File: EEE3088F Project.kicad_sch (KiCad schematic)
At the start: 2 parts, among them J1 Conn_02x16_Odd_Even, J2 Battery IN JST

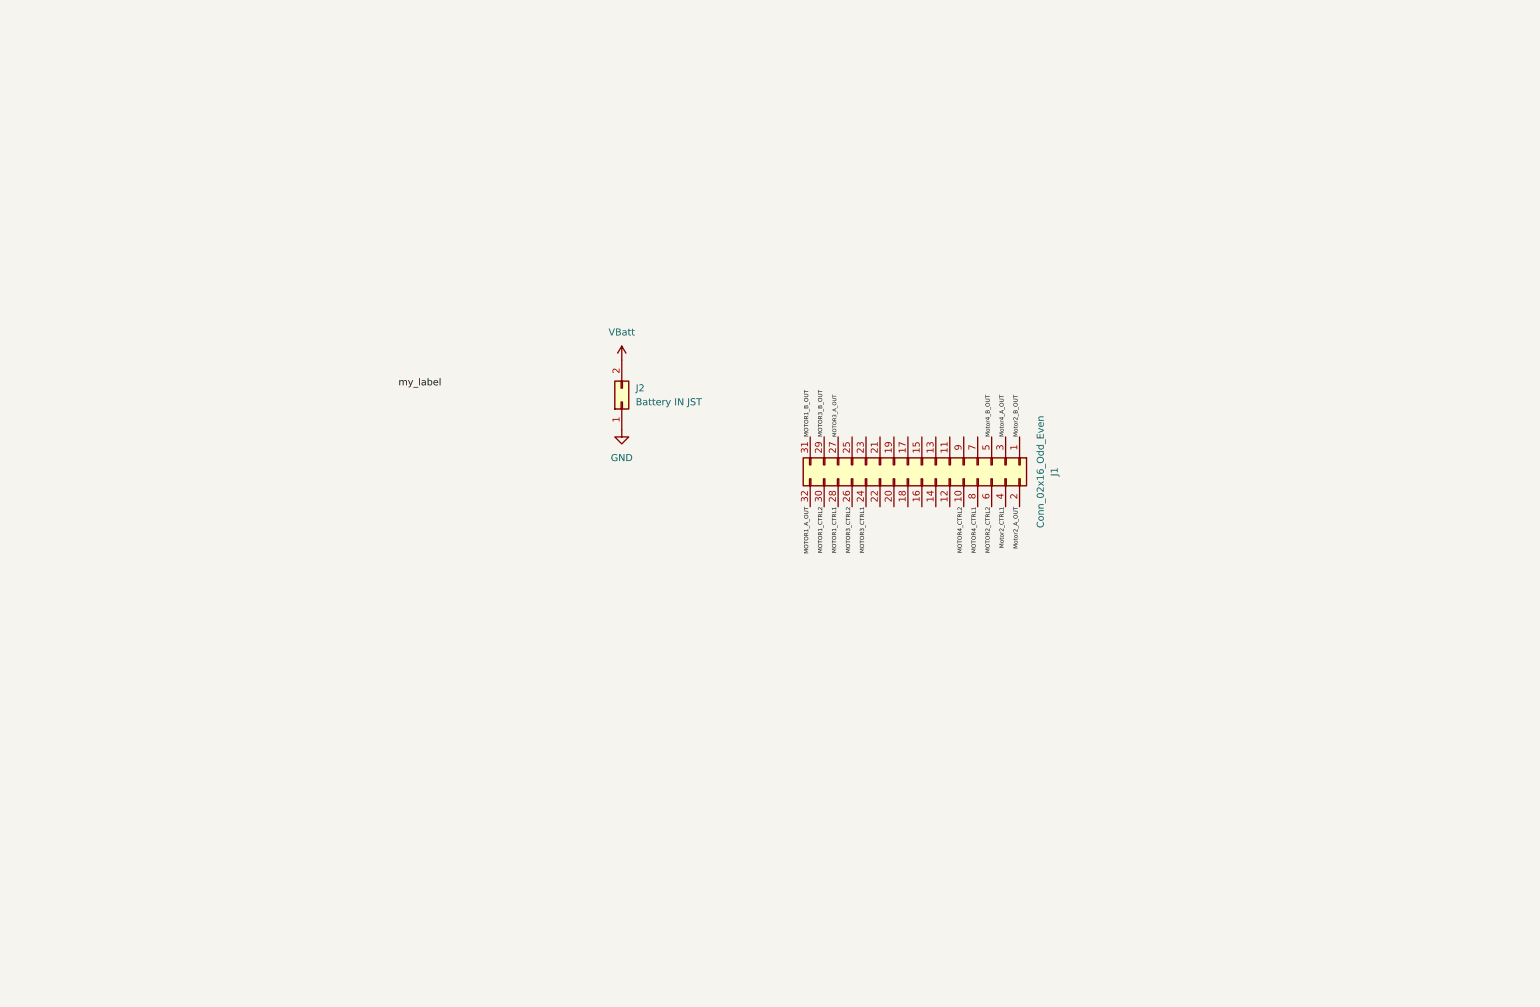
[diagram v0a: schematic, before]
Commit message: added battery charging subsection (no footprints yet)
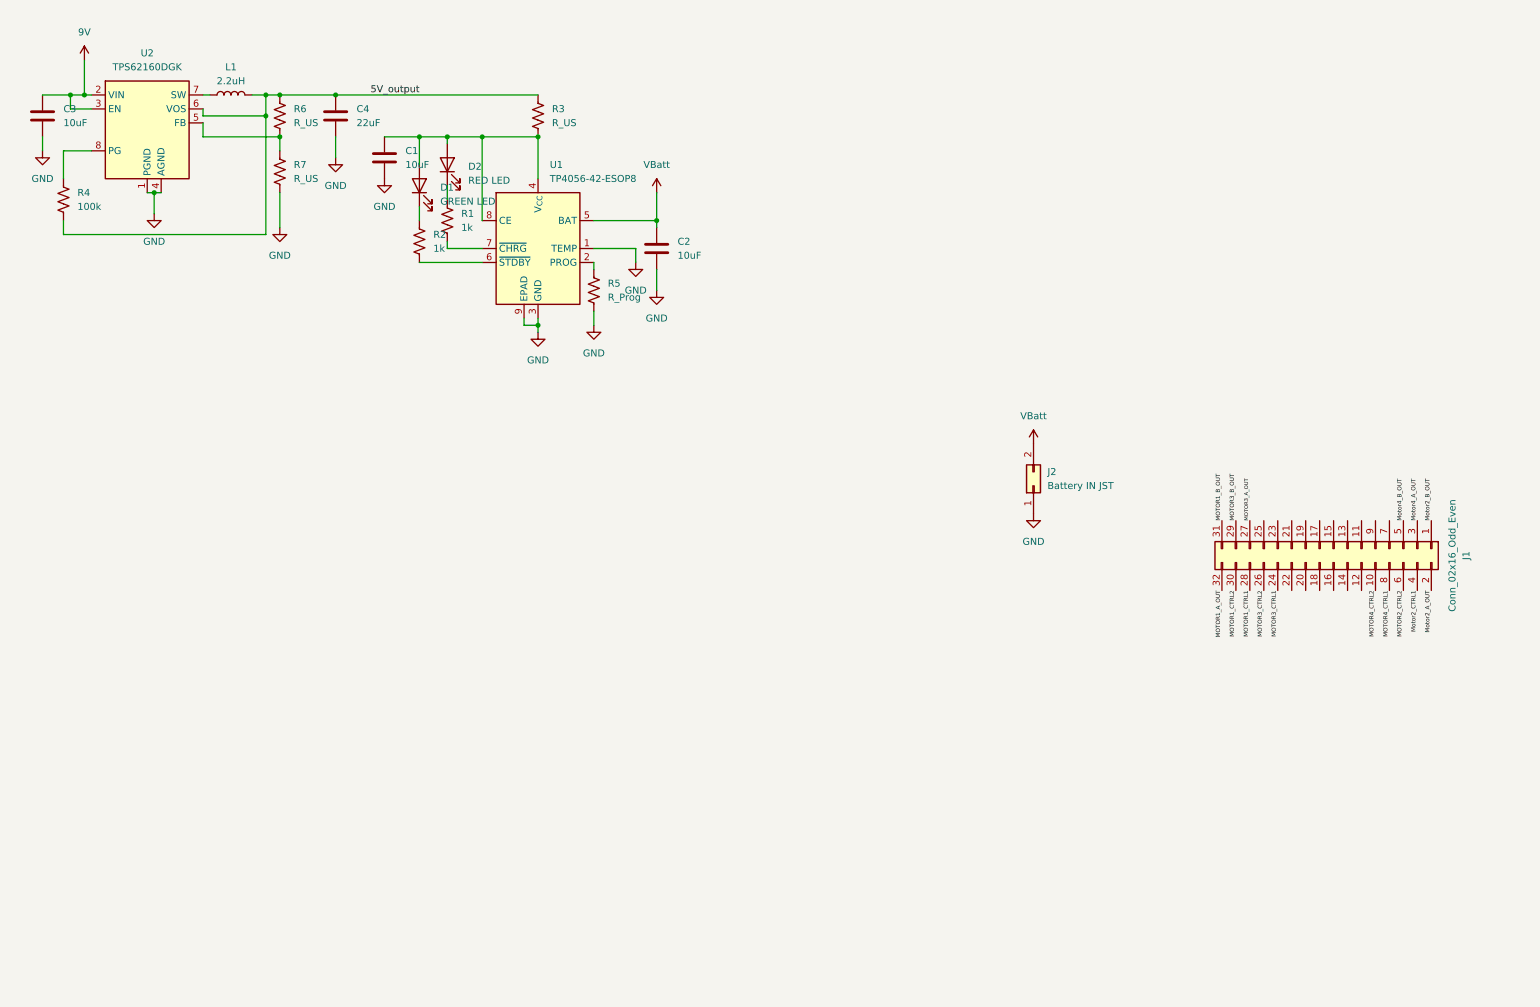
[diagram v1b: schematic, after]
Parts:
- added C1, C2, C3: 10uF, symbol Device:C
- added C4: 22uF, symbol Device:C
- added D1: GREEN LED, symbol Device:LED
- added D2: RED LED, symbol Device:LED
- added L1: 2.2uH, symbol Device:L
- added R1, R2: 1k, symbol Device:R_US
- added R3, R6, R7: R_US, symbol Device:R_US
- added R4: 100k, symbol Device:R_US
- added R5: R_Prog, symbol Device:R_US
- added U1: TP4056-42-ESOP8, Package_SO:SOIC-8-1EP_3.9x4.9mm_P1.27mm_EP2.41x3.3mm_ThermalVias, symbol Battery_Management:TP4056-42-ESOP8
- added U2: TPS62160DGK, Package_SO:MSOP-8_3x3mm_P0.65mm, symbol Regulator_Switching:TPS62160DGK
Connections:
- net GND: now also C1.1, C2.2, C3.2, C4.2, R5.2, R7.2, U1.1 (TEMP), U1.3 (GND), U1.9 (EPAD), U2.1 (PGND), U2.4 (AGND)
- net VBatt: now also C2.1, U1.5 (BAT)
- new net: D2.1 (K), R1.1
- new net: C1.2, D1.2 (A), D2.2 (A), R3.2, U1.4 (V_{CC}), U1.8 (CE)
- new net: R6.2, R7.1, U2.5 (FB)
- new net: R5.1, U1.2 (PROG)
- new net: D1.1 (K), R2.1
- new net: R2.2, U1.6 (~{STDBY})
- new net: L1.1, U2.7 (SW)
- new net: R4.1, U2.8 (PG)
- new net: R1.2, U1.7 (~{CHRG})
- new net 5V_output: C4.1, L1.2, R3.1, R4.2, R6.1, U2.6 (VOS)
- new net 9V: C3.1, U2.2 (VIN), U2.3 (EN)
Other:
- moved on the sheet: J1, J2

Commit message: Added motor driver circuits and footprints
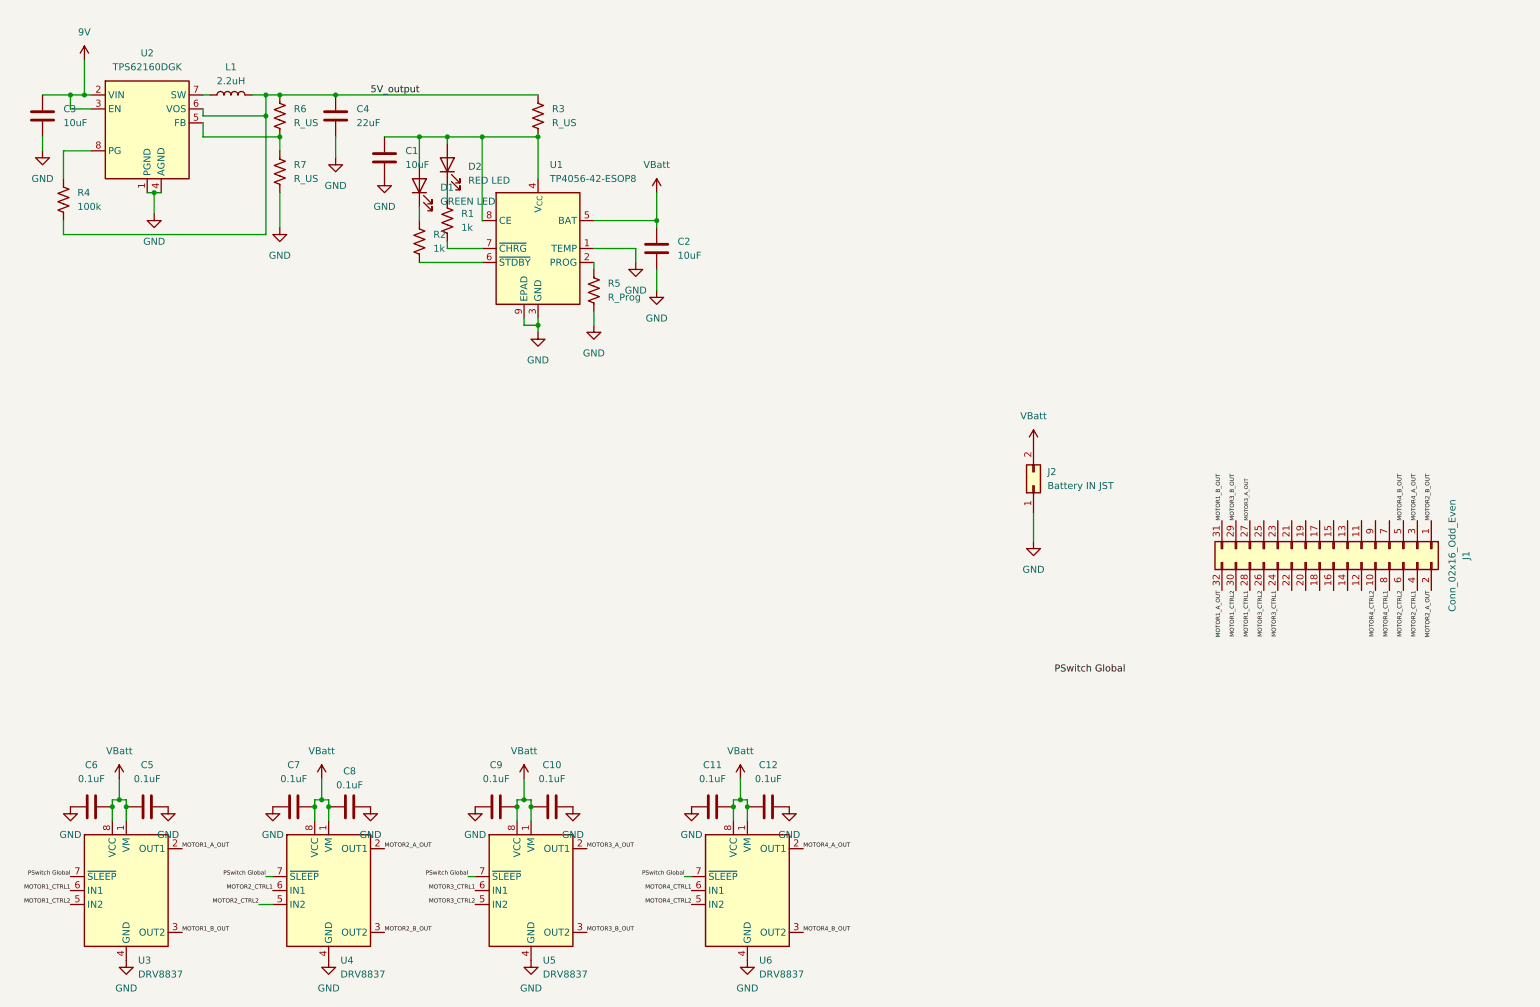
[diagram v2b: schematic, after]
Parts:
- added C10, C11, C12, C5, C6, C7, C8, C9: 0.1uF, Capacitor_SMD:C_0402_1005Metric_Pad0.74x0.62mm_HandSolder, symbol Device:C
- added U3, U4, U5, U6: DRV8837, Package_SON:WSON-8-1EP_2x2mm_P0.5mm_EP0.9x1.6mm, symbol Driver_Motor:DRV8837
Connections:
- net GND: now also C10.2, C11.1, C12.2, C5.2, C6.1, C7.1, C8.2, C9.1, U3.4 (GND), U3.9 (GND), U4.4 (GND), U4.9 (GND), U5.4 (GND), U5.9 (GND), U6.4 (GND), U6.9 (GND)
- net MOTOR1_A_OUT: now also U3.2 (OUT1)
- net MOTOR1_B_OUT : now also U3.3 (OUT2)
- net MOTOR1_CTRL1: now also U3.6 (IN1)
- net MOTOR1_CTRL2: now also U3.5 (IN2)
- net MOTOR3_A_OUT: now also U5.2 (OUT1)
- net MOTOR3_B_OUT : now also U5.3 (OUT2)
- net MOTOR3_CTRL1: now also U5.6 (IN1)
- net MOTOR3_CTRL2: now also U5.5 (IN2)
- net MOTOR4_CTRL2: now also U6.5 (IN2)
- net VBatt: now also C10.1, C11.2, C12.1, C5.1, C6.2, C7.2, C8.1, C9.2, U3.1 (VM), U3.8 (VCC), U4.1 (VM), U4.8 (VCC), U5.1 (VM), U5.8 (VCC), U6.1 (VM), U6.8 (VCC)
- net Motor2_A_OUT renamed MOTOR2_A_OUT
- net MOTOR2_A_OUT: now also U4.2 (OUT1)
- net Motor2_B_OUT renamed MOTOR2_B_OUT
- net Motor2_CTRL1 renamed MOTOR2_CTRL1
- net MOTOR2_CTRL1: now also U4.6 (IN1)
- net Motor4_A_OUT renamed MOTOR4_A_OUT
- net MOTOR4_A_OUT: now also U6.2 (OUT1)
- net Motor4_B_OUT renamed MOTOR4_B_OUT
- new net MOTOR2_B_OUT : U4.3 (OUT2)
- new net MOTOR2_CTRL2: U4.5 (IN2)
- new net MOTOR4_B_OUT : U6.3 (OUT2)
- new net MOTOR4_CTRL1: U6.6 (IN1)
- new net PSwitch Global: U3.7 (~{SLEEP}), U4.7 (~{SLEEP}), U5.7 (~{SLEEP}), U6.7 (~{SLEEP})

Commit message: started on current sensing circuit
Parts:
- added A1A2PullupCS: 3k3, symbol Device:R_Small_US
- added CurrentSensor: INA219AxDCN, Package_TO_SOT_SMD:SOT-23-8, symbol Sensor_Energy:INA219AxDCN
- renumbered U3 to M1Control, U4 to M2Control, U5 to M3Control, U6 to M4Control
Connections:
- net GND: now also CurrentSensor.3 (GND)
- net VBatt: now also A1A2PullupCS.2
- net 12C1_SCL: now reaches J1.16 (Pin_16)
- net 12C1_SDA: now reaches J1.17 (Pin_17)
- new net: A1A2PullupCS.1, CurrentSensor.7 (A0), CurrentSensor.8 (A1)
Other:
- note added: "Motor control"
- moved on the sheet: J1, J2

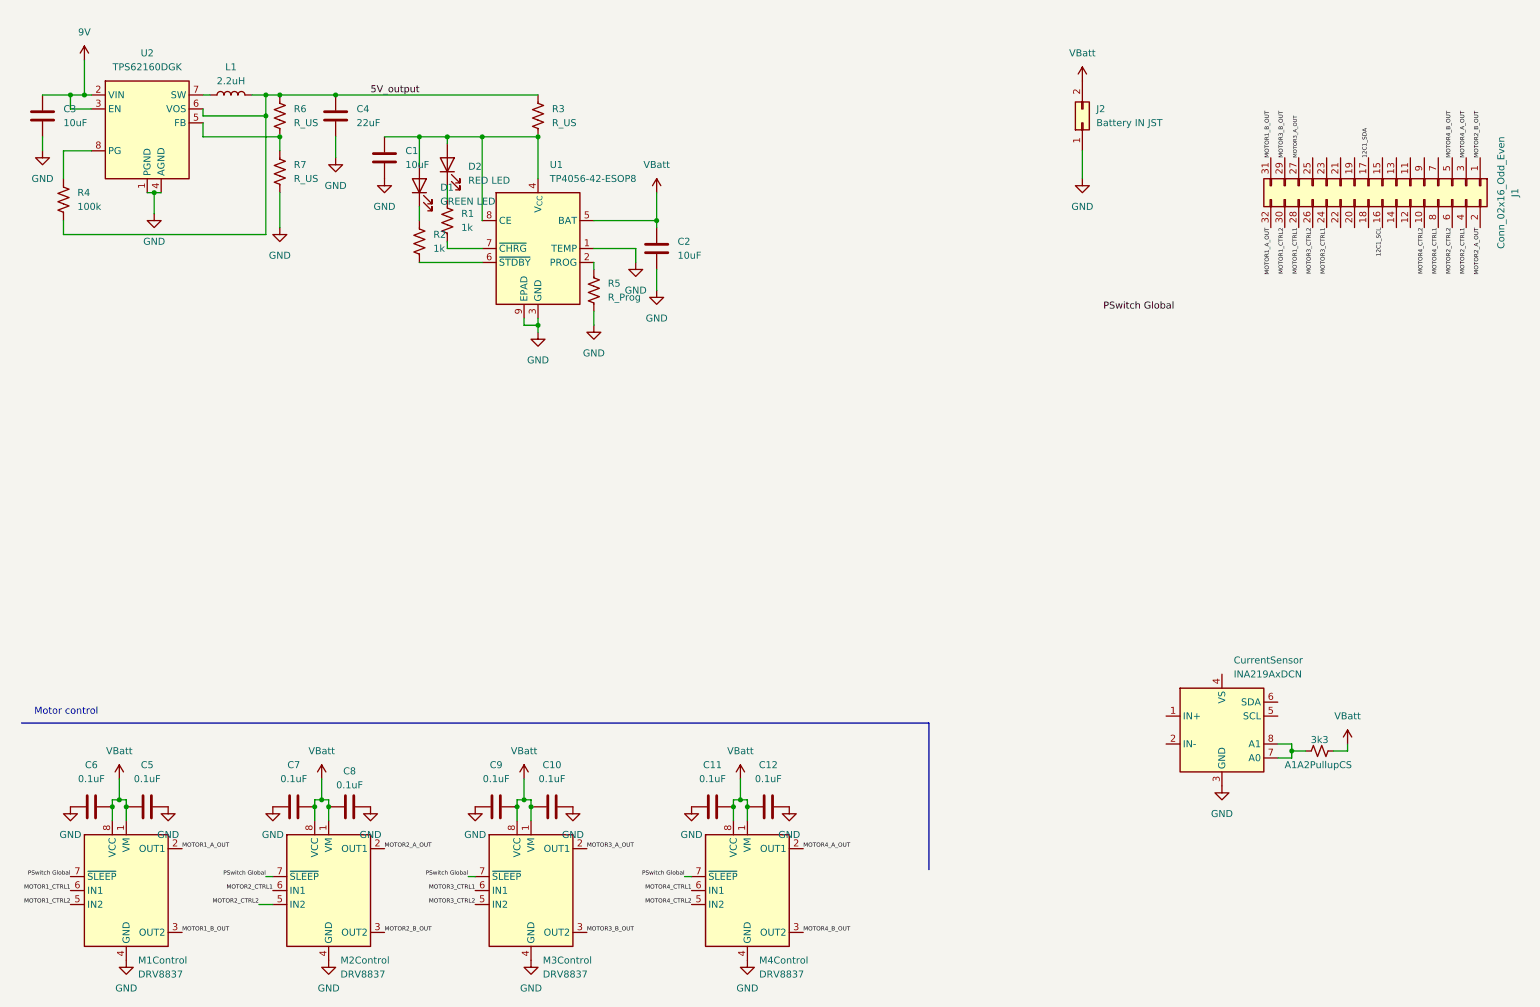
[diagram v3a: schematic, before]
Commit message: changed battery charging circuit's buck converter and added mosfet circuit for charging mode selection
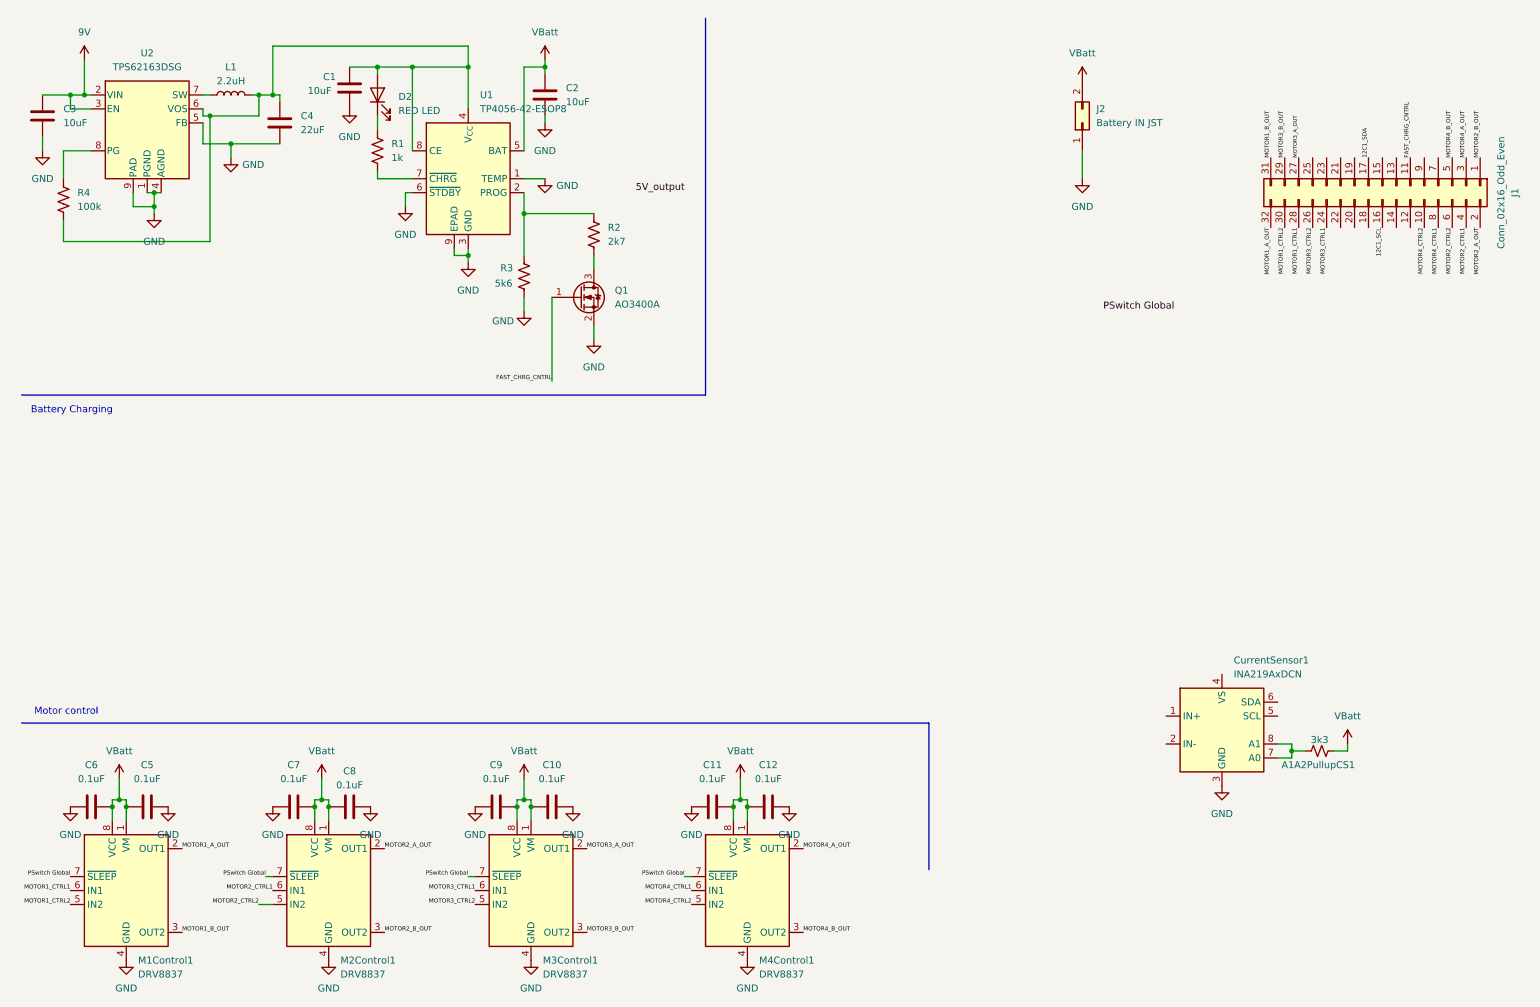
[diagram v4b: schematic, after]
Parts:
- removed D1: GREEN LED, symbol Device:LED
- removed R3, R6, R7: R_US, symbol Device:R_US
- removed U2: TPS62160DGK, Package_SO:MSOP-8_3x3mm_P0.65mm, symbol Regulator_Switching:TPS62160DGK
- added Q1: AO3400A, Package_TO_SOT_SMD:SOT-23, symbol Transistor_FET:AO3400A
- added U2: TPS62163DSG, Package_SON:WSON-8-1EP_2x2mm_P0.5mm_EP0.9x1.6mm_ThermalVias, symbol Regulator_Switching:TPS62163DSG
- C1, C2, C3: footprint (none) -> Capacitor_SMD:C_0805_2012Metric_Pad1.18x1.45mm_HandSolder
- C4: footprint (none) -> Capacitor_SMD:C_1206_3216Metric_Pad1.33x1.80mm_HandSolder
- D2: footprint (none) -> LED_SMD:LED_0805_2012Metric
- L1: footprint (none) -> Inductor_SMD:L_Taiyo-Yuden_MD-3030
- R1, R4: footprint (none) -> Resistor_SMD:R_0603_1608Metric_Pad0.98x0.95mm_HandSolder
- R2: value 1k -> 2k7; footprint (none) -> Resistor_SMD:R_0603_1608Metric_Pad0.98x0.95mm_HandSolder
- R3: renamed from R5; value R_Prog -> 5k6; footprint (none) -> Resistor_SMD:R_0603_1608Metric_Pad0.98x0.95mm_HandSolder
- renumbered A1A2PullupCS to A1A2PullupCS1, CurrentSensor to CurrentSensor1, M1Control to M1Control1, M2Control to M2Control1, M3Control to M3Control1, M4Control to M4Control1
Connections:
- net 5V_output: no longer C4.1, L1.2, R4.2
- net 9V: now also U2.2 (VIN), U2.3 (EN)
- net GND: now also U1.6 (~{STDBY}), Q1.2 (S), U2.1 (PGND), U2.4 (AGND), U2.5 (FB), U2.9 (PAD)
- net at C1.2, D2.2 (A), U1.4 (V_{CC})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: now also C4.1, L1.2, R4.2, U2.6 (VOS)
- net FAST_CHRG_CNTRL: now reaches J1.11 (Pin_11)
- net FAST_CHRG_CNTRL: now also Q1.1 (G)
- net at R3.1, U1.2 (PROG): now also R2.1
- net at R2.2: now also Q1.3 (D); no longer U1.6 (~{STDBY})
- net at L1.1: now also U2.7 (SW)
- net at R4.1: now also U2.8 (PG)
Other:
- note added: "Battery Charging"
- moved on the sheet: C1, C2, C4, D2, R1, R3, U1
